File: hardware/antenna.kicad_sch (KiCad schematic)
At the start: 8 parts

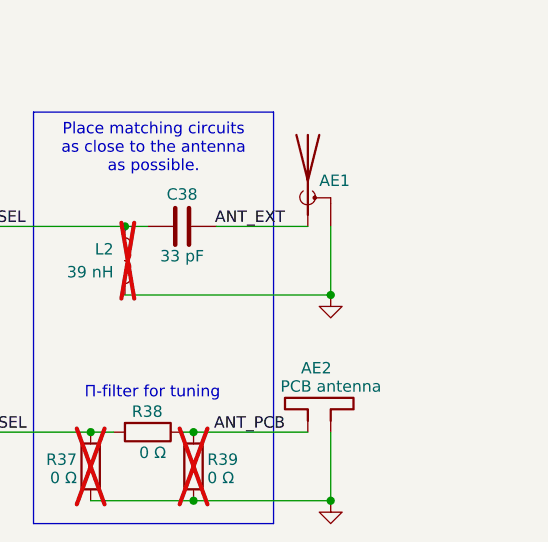
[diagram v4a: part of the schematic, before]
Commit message: HW: Cleanup schematic
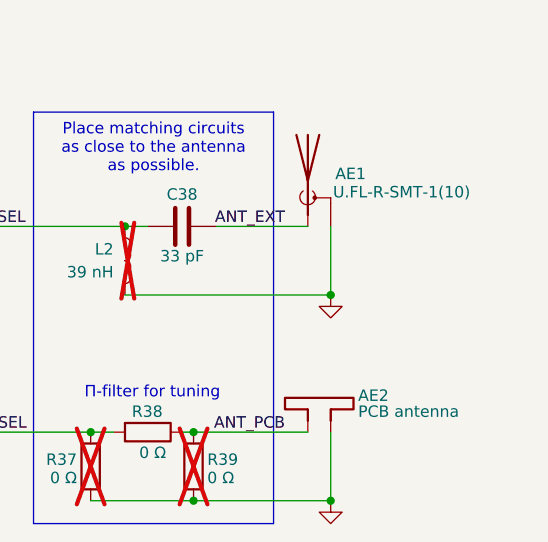
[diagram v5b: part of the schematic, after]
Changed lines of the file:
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@@
 		(dnp no)
 		(property "Reference" "AE2"
-			(at 146.558 104.648 0)
+			(at 152.908 107.696 0)
 			(effects
 				(font
@@
 		)
 		(property "Value" "PCB antenna"
-			(at 144.272 106.68 0)
+			(at 152.908 109.474 0)
 			(effects
 				(font
@@
 		(dnp no)
 		(fields_autoplaced yes)
-		(property "Reference" "#PWR060"
+		(property "Reference" "#PWR054"
 			(at 149.86 125.73 0)
 			(effects
@@
 			(project "iida_devkit"
 				(path "/b12a6e25-97fb-4aba-bc96-af8db389bb9a/6e456e95-dbda-43fc-b148-815c3be21ba0"
-					(reference "#PWR060")
+					(reference "#PWR054")
 					(unit 1)
 				)
@@
 		(dnp no)
 		(fields_autoplaced yes)
-		(property "Reference" "#PWR059"
+		(property "Reference" "#PWR053"
 			(at 149.86 102.87 0)
 			(effects
@@
 			(project "iida_devkit"
 				(path "/b12a6e25-97fb-4aba-bc96-af8db389bb9a/6e456e95-dbda-43fc-b148-815c3be21ba0"
-					(reference "#PWR059")
+					(reference "#PWR053")
 					(unit 1)
 				)
@@
 		(dnp no)
 		(property "Reference" "AE1"
-			(at 148.59 83.82 0)
+			(at 150.368 83.058 0)
 			(effects
 				(font
@@
 		)
 		(property "Value" "U.FL-R-SMT-1(10)"
-			(at 150.495 85.725 0)
+			(at 150.114 85.09 0)
 			(effects
 				(font
@@
 				)
 				(justify left)
-				(hide yes)
-			)
-		)
+			)
+		)

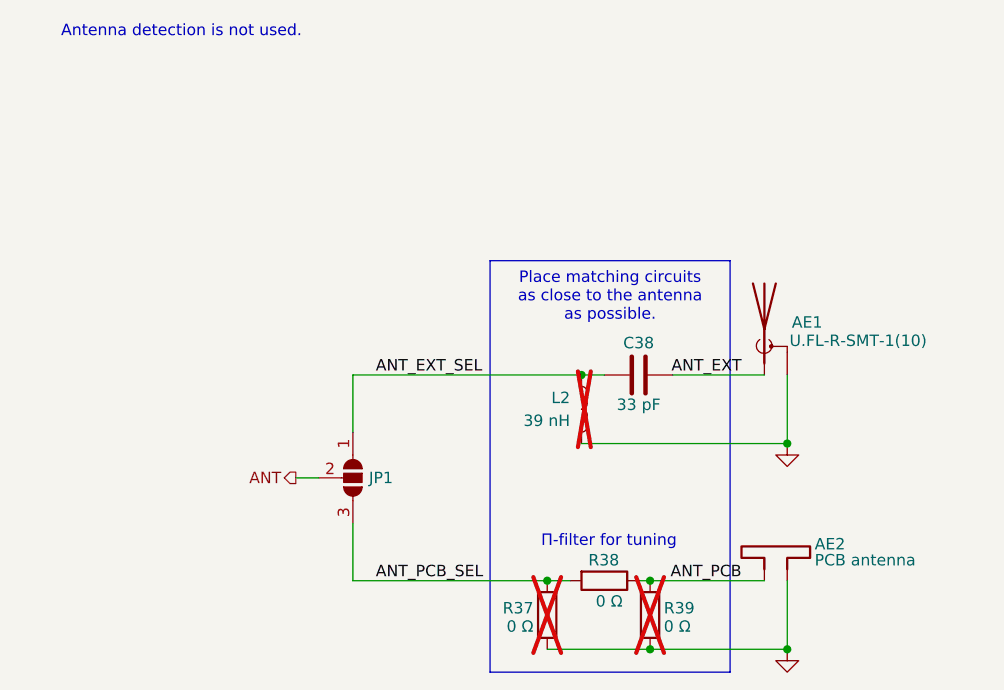
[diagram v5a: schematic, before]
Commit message: HW: Add bulk cap to VBAT
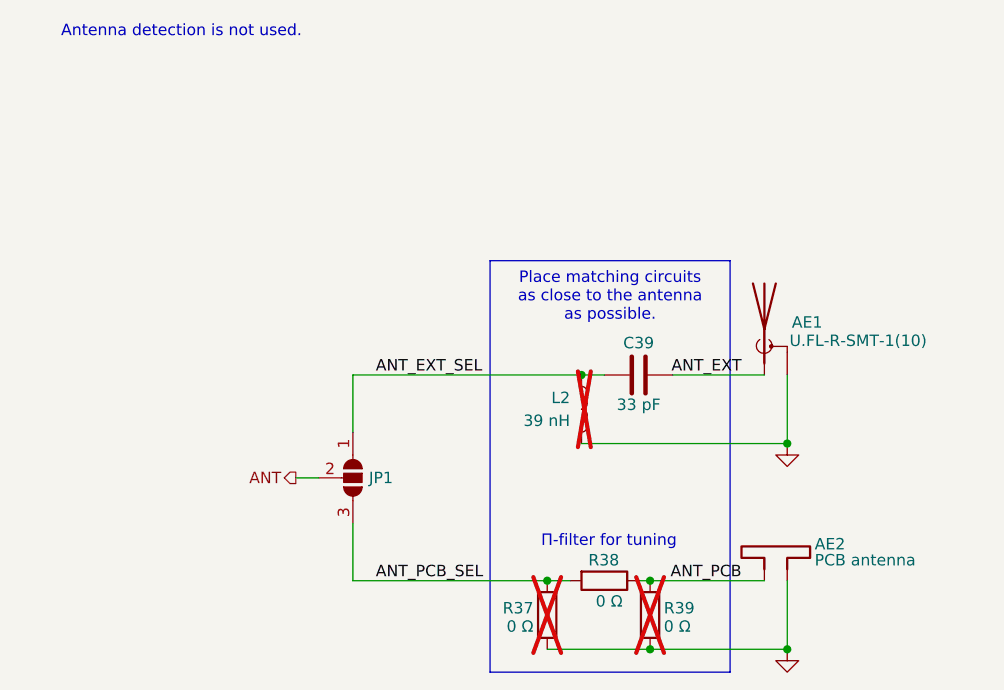
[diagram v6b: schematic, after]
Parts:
- renumbered C38 to C39
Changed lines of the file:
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@@
 		(on_board yes)
 		(dnp no)
-		(property "Reference" "C38"
+		(property "Reference" "C39"
 			(at 133.35 85.344 90)
 			(effects
@@
 			(project "iida_devkit"
 				(path "/b12a6e25-97fb-4aba-bc96-af8db389bb9a/6e456e95-dbda-43fc-b148-815c3be21ba0"
-					(reference "C38")
+					(reference "C39")
 					(unit 1)
 				)
@@
 		(dnp no)
 		(fields_autoplaced yes)
-		(property "Reference" "#PWR054"
+		(property "Reference" "#PWR055"
 			(at 149.86 125.73 0)
 			(effects
@@
 			(project "iida_devkit"
 				(path "/b12a6e25-97fb-4aba-bc96-af8db389bb9a/6e456e95-dbda-43fc-b148-815c3be21ba0"
-					(reference "#PWR054")
+					(reference "#PWR055")
 					(unit 1)
 				)
@@
 		(dnp no)
 		(fields_autoplaced yes)
-		(property "Reference" "#PWR053"
+		(property "Reference" "#PWR054"
 			(at 149.86 102.87 0)
 			(effects
@@
 			(project "iida_devkit"
 				(path "/b12a6e25-97fb-4aba-bc96-af8db389bb9a/6e456e95-dbda-43fc-b148-815c3be21ba0"
-					(reference "#PWR053")
-					(unit 1)
-				)
+					(reference "#PWR054")
+					(unit 1)
+				)

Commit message: HW: Refine schema
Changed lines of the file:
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@@
 	)
 	(hierarchical_label "ANT"
-		(shape output)
+		(shape bidirectional)
 		(at 95.25 100.33 180)
 		(fields_autoplaced yes)

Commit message: HW: Fix components
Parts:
- renumbered R37 to R38, R38 to R39, R39 to R40
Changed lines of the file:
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@@
 		(on_board yes)
 		(dnp no)
-		(property "Reference" "R38"
+		(property "Reference" "R39"
 			(at 127.762 109.474 90)
 			(effects
@@
 			(project "iida_devkit"
 				(path "/b12a6e25-97fb-4aba-bc96-af8db389bb9a/6e456e95-dbda-43fc-b148-815c3be21ba0"
-					(reference "R38")
+					(reference "R39")
 					(unit 1)
 				)
@@
 		(on_board yes)
 		(dnp yes)
-		(property "Reference" "R37"
+		(property "Reference" "R38"
 			(at 121.666 114.808 0)
 			(effects
@@
 			(project "iida_devkit"
 				(path "/b12a6e25-97fb-4aba-bc96-af8db389bb9a/6e456e95-dbda-43fc-b148-815c3be21ba0"
-					(reference "R37")
+					(reference "R38")
 					(unit 1)
 				)
@@
 		(on_board yes)
 		(dnp yes)
-		(property "Reference" "R39"
+		(property "Reference" "R40"
 			(at 136.144 114.808 0)
 			(effects
@@
 			(project "iida_devkit"
 				(path "/b12a6e25-97fb-4aba-bc96-af8db389bb9a/6e456e95-dbda-43fc-b148-815c3be21ba0"
-					(reference "R39")
+					(reference "R40")
 					(unit 1)
 				)
